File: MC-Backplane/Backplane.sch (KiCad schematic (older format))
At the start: 4 parts

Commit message: added reverse polarity protection circuit and fuse
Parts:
- removed R?: R_load, symbol Device:R_Small_US
- added F?: Fuse, symbol Device:Fuse
- D?: value BZX84C9V1-7-F -> Zener BZX84C9V1-7-F
- R?: value R1 -> 3k; footprint (none) -> Resistor_SMD:R_0201_0603Metric
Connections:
- net labels added: 24v
- net labels removed: +24V
- wire segments 14 -> 21
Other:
- note added: "Global reset to/from all cards and DSP\nFO enable b/w DSP and FO card only"
- note added: "If 0603 is used, minimum of 2.2k Ohm should be used.\n"
- note added: "Reverse Polarity Protection Circuit"
- moved on the sheet: D?, Q?, R?
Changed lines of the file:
@@
 F0 "GateDriveSlots" 50
 F1 "GateDriveSlots.sch" 50
+F2 "24vP" I L 2000 5350 50
 $EndSheet
 $Sheet
@@
 F0 "DeltaSigmaSlots" 50
 F1 "DeltaSigmasSlots.sch" 50
+F2 "24vP" I L 5000 5350 50
 $EndSheet
 $Sheet
-S 8750 5200 950  450
+S 8550 5250 950  450
 U 61E8CB26
 F0 "ADCSlots" 50
 F1 "ADCSlots.sch" 50
+F2 "24vP" I L 8550 5350 50
 $EndSheet
 $Sheet
-S 2200 2350 1000 450
+S 7900 2100 950  1900
 U 61E8CBE3
 F0 "DSPSlot" 50
 F1 "DSPSlot.sch" 50
+F2 "24vP" I L 7900 2200 50
 $EndSheet
-$Comp
-L power:+24V #PWR?
-U 1 1 61E8D5B6
-P 7350 1350
-F 0 "#PWR?" H 7350 1200 50  0001 C CNN
-F 1 "+24V" H 7365 1523 50  0000 C CNN
-F 2 "" H 7350 1350 50  0001 C CNN
-F 3 "" H 7350 1350 50  0001 C CNN
-	1    7350 1350
-	1    0    0    -1
-$EndComp
 $Comp
 L Device:Q_PMOS_DGS Q?
 U 1 1 61EB5F9E
-P 8500 1550
-F 0 "Q?" V 8842 1550 50  0000 C CNN
-F 1 "TSM3401CX RFG" V 8751 1550 50  0000 C CNN
-F 2 "" H 8700 1650 50  0001 C CNN
-F 3 "https://www.digikey.com/en/products/detail/taiwan-semiconductor-corporation/TSM3401CX-RFG/7360318" H 8500 1550 50  0001 C CNN
-	1    8500 1550
+P 2850 2300
+F 0 "Q?" V 3192 2300 50  0000 C CNN
+F 1 "TSM3401CX RFG" V 3101 2300 50  0000 C CNN
+F 2 "" H 3050 2400 50  0001 C CNN
+F 3 "https://www.digikey.com/en/products/detail/taiwan-semiconductor-corporation/TSM3401CX-RFG/7360318" H 2850 2300 50  0001 C CNN
+	1    2850 2300
 	0    -1   -1   0
 $EndComp
@@
 L Device:D_Zener D?
 U 1 1 61EB8C1B
-P 9350 1750
-F 0 "D?" V 9304 1830 50  0000 L CNN
-F 1 "BZX84C9V1-7-F" V 9395 1830 50  0000 L CNN
-F 2 "" H 9350 1750 50  0001 C CNN
-F 3 "https://www.digikey.com/en/products/detail/diodes-incorporated/BZX84C9V1-7-F/717755" H 9350 1750 50  0001 C CNN
-	1    9350 1750
+P 3700 2500
+F 0 "D?" V 3654 2580 50  0000 L CNN
+F 1 "Zener BZX84C9V1-7-F" V 3745 2580 50  0000 L CNN
+F 2 "" H 3700 2500 50  0001 C CNN
+F 3 "https://www.digikey.com/en/products/detail/diodes-incorporated/BZX84C9V1-7-F/717755" H 3700 2500 50  0001 C CNN
+	1    3700 2500
 	0    1    1    0
 $EndComp
 $Comp
 L Device:R_Small_US R?
-U 1 1 61EBA674
-P 10250 2100
-F 0 "R?" H 10318 2146 50  0000 L CNN
-F 1 "R_load" H 10318 2055 50  0000 L CNN
-F 2 "" H 10250 2100 50  0001 C CNN
-F 3 "~" H 10250 2100 50  0001 C CNN
-	1    10250 2100
-	1    0    0    -1
-$EndComp
-$Comp
-L Device:R_Small_US R?
 U 1 1 61EBB5D2
-P 8500 2400
-F 0 "R?" H 8568 2446 50  0000 L CNN
-F 1 "R1" H 8568 2355 50  0000 L CNN
-F 2 "" H 8500 2400 50  0001 C CNN
-F 3 "~" H 8500 2400 50  0001 C CNN
-	1    8500 2400
+P 2850 3150
+F 0 "R?" H 2918 3196 50  0000 L CNN
+F 1 "3k" H 2918 3105 50  0000 L CNN
+F 2 "Resistor_SMD:R_0201_0603Metric" H 2850 3150 50  0001 C CNN
+F 3 "~" H 2850 3150 50  0001 C CNN
+	1    2850 3150
 	1    0    0    -1
 $EndComp
 Wire Wire Line
-	8500 1750 8500 2000
+	2850 2500 2850 2750
 Wire Wire Line
-	9350 1900 9350 2000
+	3700 2650 3700 2750
 Wire Wire Line
-	9350 2000 8500 2000
-Connection ~ 8500 2000
+	3700 2750 2850 2750
+Connection ~ 2850 2750
 Wire Wire Line
-	8500 2000 8500 2300
+	2850 2750 2850 3050
 Wire Wire Line
-	9350 1600 9350 1450
+	3700 2350 3700 2200
 Wire Wire Line
-	9350 1450 8700 1450
+	3700 2200 3050 2200
+Connection ~ 3700 2200
 Wire Wire Line
-	9350 1450 10250 1450
-Wire Wire Line
-	10250 1450 10250 2000
-Connection ~ 9350 1450
-Wire Wire Line
-	8300 1450 7350 1450
-Wire Wire Line
-	7350 1450 7350 1350
-Wire Wire Line
-	10250 2750 8500 2750
-Wire Wire Line
-	8500 2750 8500 2500
-Wire Wire Line
-	10250 2200 10250 2750
-Wire Wire Line
-	8500 2750 8500 2850
-Connection ~ 8500 2750
+	2650 2200 2250 2200
 $Comp
-L power:GND #PWR?
+L power:GND #PWR0101
 U 1 1 61EBD36B
-P 8500 2850
-F 0 "#PWR?" H 8500 2600 50  0001 C CNN
-F 1 "GND" H 8505 2677 50  0000 C CNN
-F 2 "" H 8500 2850 50  0001 C CNN
-F 3 "" H 8500 2850 50  0001 C CNN
-	1    8500 2850
+P 2850 3600
+F 0 "#PWR0101" H 2850 3350 50  0001 C CNN
+F 1 "GND" H 2855 3427 50  0000 C CNN
+F 2 "" H 2850 3600 50  0001 C CNN
+F 3 "" H 2850 3600 50  0001 C CNN
+	1    2850 3600
 	1    0    0    -1
 $EndComp
-Text Notes 5800 3600 0    50   ~ 0
+Text Notes 800  1300 0    50   ~ 0
 RDS of PMOS needs to be really small like miliohms.\n\nDrain current needs to be larger than what the load requires.\nVDS needs to be larger than the source voltage by a significant amount. 24V so around  45V-60V.\n\nThe Zener diode needs a voltage rating of just under VDS of the mosfet. \n\nnot sure about the resistors.
+Wire Wire Line
+	2850 3250 2850 3600
+Text Notes 600  3000 0    50   ~ 0
+If 0603 is used, minimum of 2.2k Ohm should be used.\n
+Text GLabel 1700 2200 0    50   Input ~ 0
+24v
+$Comp
+L Device:Fuse F?
+U 1 1 61F00499
+P 2100 2200
+F 0 "F?" V 1903 2200 50  0000 C CNN
+F 1 "Fuse" V 1994 2200 50  0000 C CNN
+F 2 "" V 2030 2200 50  0001 C CNN
+F 3 "~" H 2100 2200 50  0001 C CNN
+	1    2100 2200
+	0    1    1    0
+$EndComp
+Wire Wire Line
+	1950 2200 1700 2200
+Text Notes 2250 1800 0    50   ~ 0
+Reverse Polarity Protection Circuit
+Text Notes 8500 900  0    50   ~ 0
+Global reset to/from all cards and DSP\nFO enable b/w DSP and FO card only
+Wire Wire Line
+	3700 2200 4750 2200
+Wire Wire Line
+	4750 2200 4750 4250
+Wire Wire Line
+	1200 4250 1200 5350
+Wire Wire Line
+	1200 5350 2000 5350
+Connection ~ 4750 4250
+Wire Wire Line
+	4750 4250 1200 4250
+Wire Wire Line
+	4750 5350 5000 5350
+Wire Wire Line
+	4750 4250 4750 4950
+Wire Wire Line
+	4750 4950 8150 4950
+Wire Wire Line
+	8150 4950 8150 5350
+Wire Wire Line
+	8150 5350 8550 5350
+Connection ~ 4750 4950
+Wire Wire Line
+	4750 4950 4750 5350
+Wire Wire Line
+	4750 2200 7900 2200
+Connection ~ 4750 2200
 $EndSCHEMATC

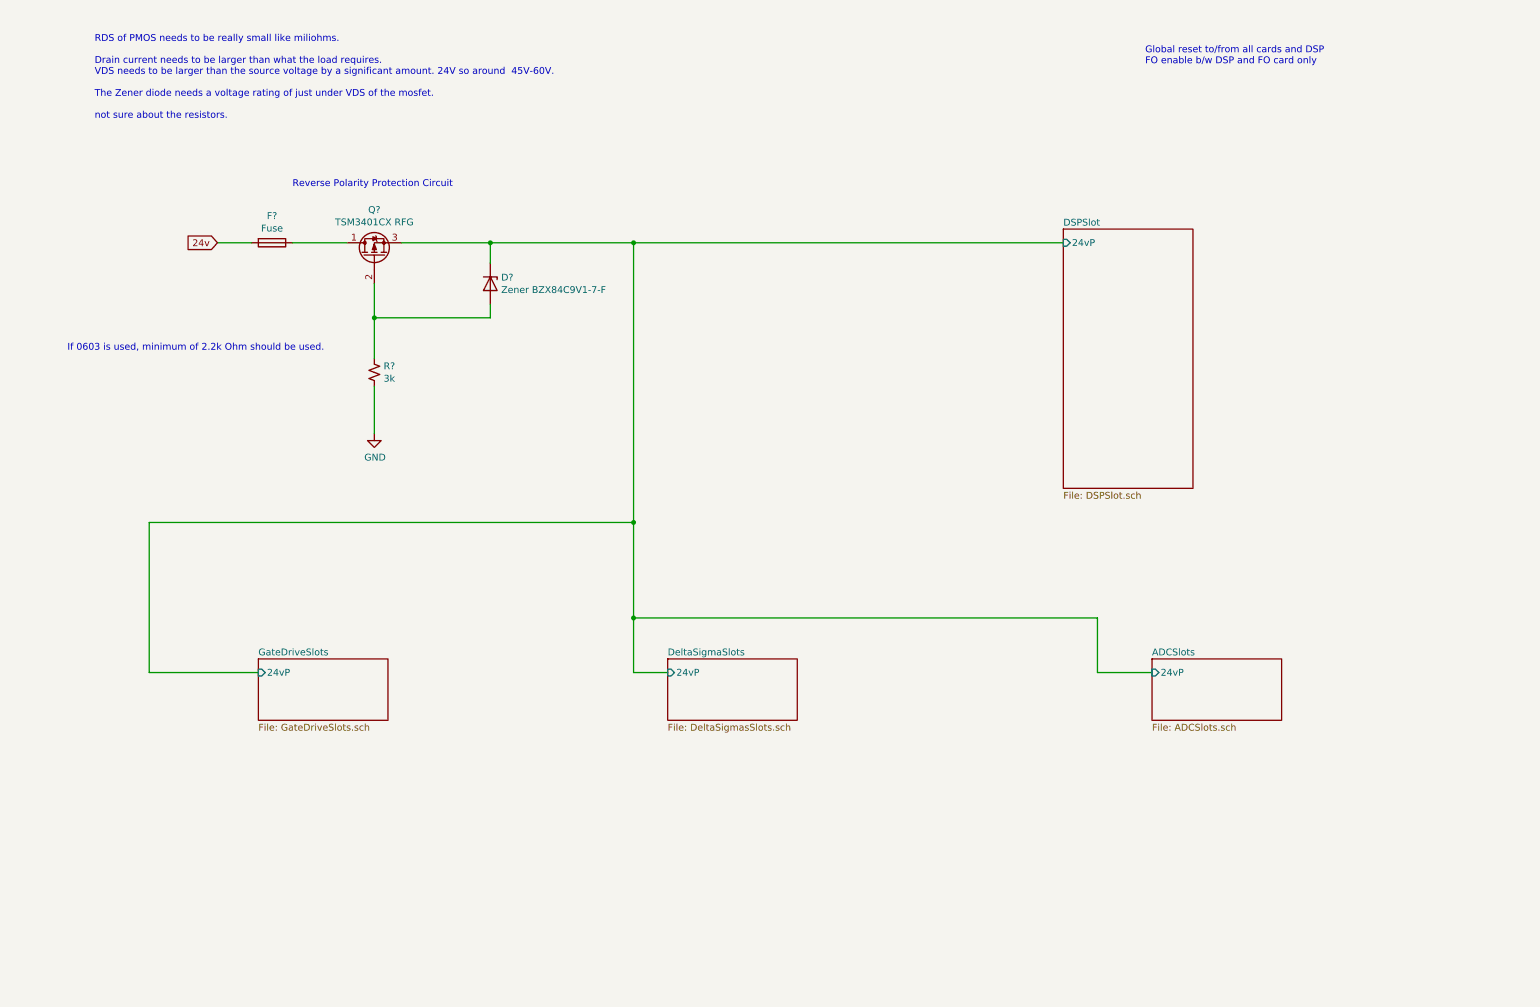
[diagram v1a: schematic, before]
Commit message: pmos swap, fuse cartridge, power conn
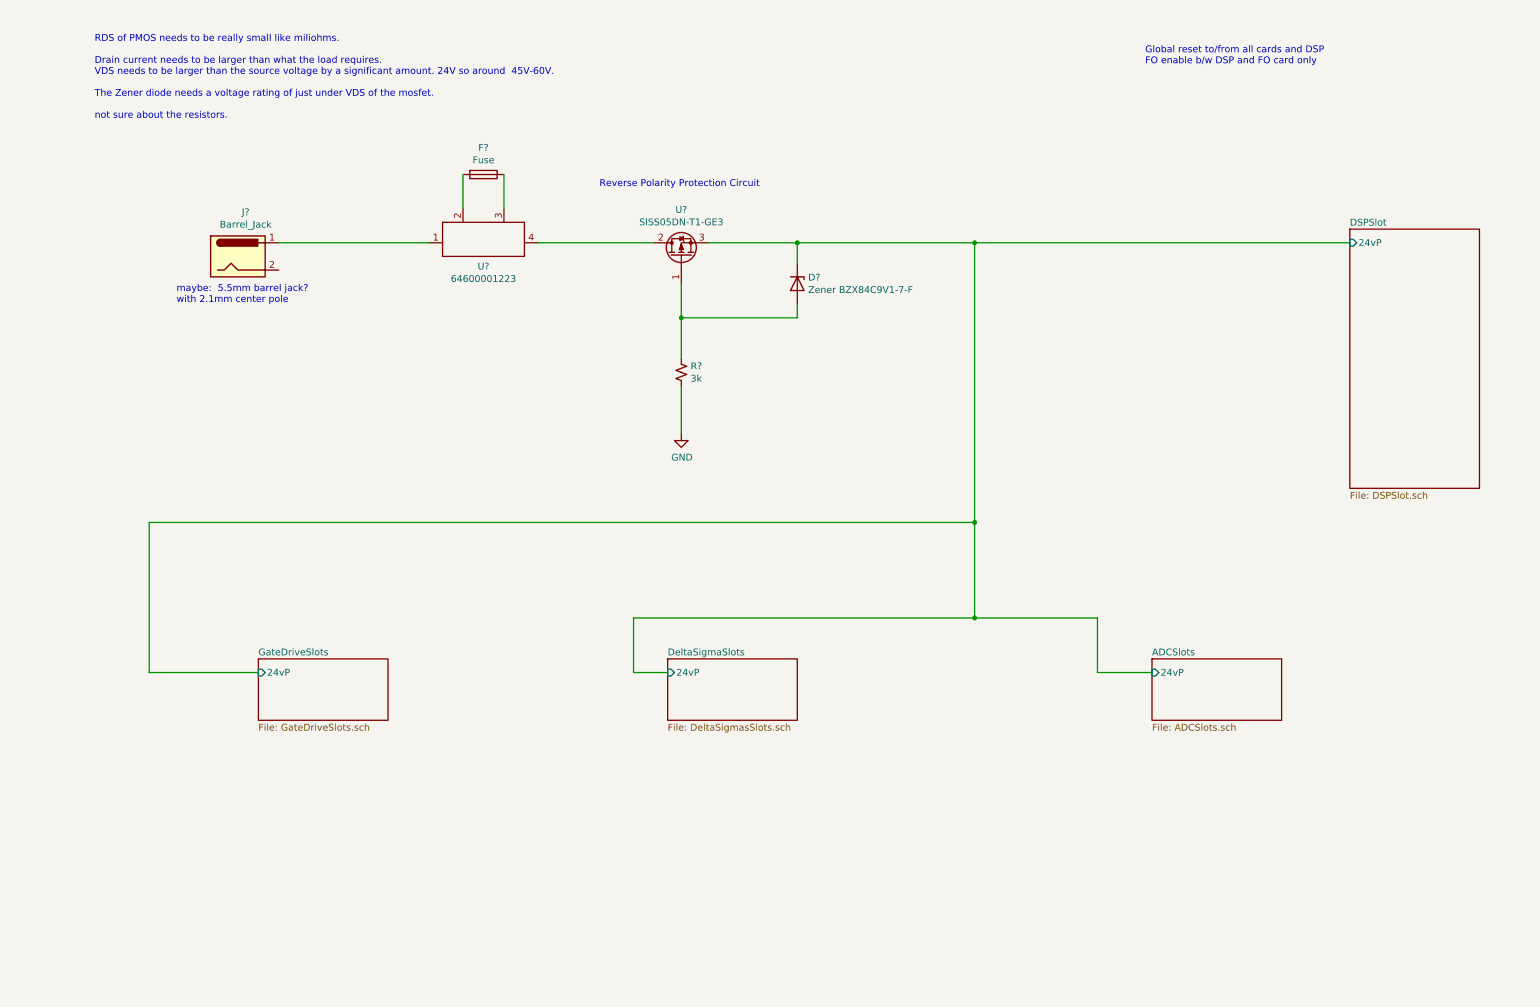
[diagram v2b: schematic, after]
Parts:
- removed F?: Fuse, symbol Device:Fuse
- removed Q?: TSM3401CX RFG, symbol Device:Q_PMOS_DGS
- added F?: Fuse, symbol Device:Fuse
- added J?: Barrel_Jack, symbol Connector:Barrel_Jack
- added U?: 64600001223, symbol MC-Backplane:64600001223
- added U?: SISS05DN-T1-GE3, symbol MC-Backplane:SISS05DN-T1-GE3
- R?: footprint Resistor_SMD:R_0201_0603Metric -> Resistor_SMD:R_1206_3216Metric
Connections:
- net ADCSlots/24vP: now also U?.3 (Source)
- net at D?.2 (A), R?.1: now also U?.1 (G)
- new net: J?.1, U?.1 (in)
- new net: F?.2, U?.2 (a)
- new net: F?.1, U?.3 (b)
- new net: U?.2 (Drain), U?.4 (out)
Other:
- note added: "maybe: 5.5mm barrel jack? \nwith 2.1mm center pole"
- note removed: "If 0603 is used, minimum of 2.2k Ohm should be used.\n"
- moved on the sheet: D?, R?
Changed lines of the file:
@@
 F2 "24vP" I L 8550 5350 50
 $EndSheet
-$Sheet
-S 7900 2100 950  1900
-U 61E8CBE3
-F0 "DSPSlot" 50
-F1 "DSPSlot.sch" 50
-F2 "24vP" I L 7900 2200 50
-$EndSheet
-$Comp
-L Device:Q_PMOS_DGS Q?
-U 1 1 61EB5F9E
-P 2850 2300
-F 0 "Q?" V 3192 2300 50  0000 C CNN
-F 1 "TSM3401CX RFG" V 3101 2300 50  0000 C CNN
-F 2 "" H 3050 2400 50  0001 C CNN
-F 3 "https://www.digikey.com/en/products/detail/taiwan-semiconductor-corporation/TSM3401CX-RFG/7360318" H 2850 2300 50  0001 C CNN
-	1    2850 2300
-	0    -1   -1   0
-$EndComp
 $Comp
 L Device:D_Zener D?
 U 1 1 61EB8C1B
-P 3700 2500
-F 0 "D?" V 3654 2580 50  0000 L CNN
-F 1 "Zener BZX84C9V1-7-F" V 3745 2580 50  0000 L CNN
-F 2 "" H 3700 2500 50  0001 C CNN
-F 3 "https://www.digikey.com/en/products/detail/diodes-incorporated/BZX84C9V1-7-F/717755" H 3700 2500 50  0001 C CNN
-	1    3700 2500
+P 5950 2500
+F 0 "D?" V 5904 2580 50  0000 L CNN
+F 1 "Zener BZX84C9V1-7-F" V 5995 2580 50  0000 L CNN
+F 2 "" H 5950 2500 50  0001 C CNN
+F 3 "https://www.digikey.com/en/products/detail/diodes-incorporated/BZX84C9V1-7-F/717755" H 5950 2500 50  0001 C CNN
+	1    5950 2500
 	0    1    1    0
 $EndComp
@@
 L Device:R_Small_US R?
 U 1 1 61EBB5D2
-P 2850 3150
-F 0 "R?" H 2918 3196 50  0000 L CNN
-F 1 "3k" H 2918 3105 50  0000 L CNN
-F 2 "Resistor_SMD:R_0201_0603Metric" H 2850 3150 50  0001 C CNN
-F 3 "~" H 2850 3150 50  0001 C CNN
-	1    2850 3150
+P 5100 3150
+F 0 "R?" H 5168 3196 50  0000 L CNN
+F 1 "3k" H 5168 3105 50  0000 L CNN
+F 2 "Resistor_SMD:R_1206_3216Metric" H 5100 3150 50  0001 C CNN
+F 3 "~" H 5100 3150 50  0001 C CNN
+	1    5100 3150
 	1    0    0    -1
 $EndComp
 Wire Wire Line
-	2850 2500 2850 2750
+	5100 2500 5100 2750
 Wire Wire Line
-	3700 2650 3700 2750
+	5950 2650 5950 2750
 Wire Wire Line
-	3700 2750 2850 2750
-Connection ~ 2850 2750
+	5950 2750 5100 2750
+Connection ~ 5100 2750
 Wire Wire Line
-	2850 2750 2850 3050
+	5100 2750 5100 3050
 Wire Wire Line
-	3700 2350 3700 2200
+	5950 2350 5950 2200
 Wire Wire Line
-	3700 2200 3050 2200
-Connection ~ 3700 2200
-Wire Wire Line
-	2650 2200 2250 2200
+	5950 2200 5300 2200
+Connection ~ 5950 2200
 $Comp
 L power:GND #PWR0101
 U 1 1 61EBD36B
-P 2850 3600
-F 0 "#PWR0101" H 2850 3350 50  0001 C CNN
-F 1 "GND" H 2855 3427 50  0000 C CNN
-F 2 "" H 2850 3600 50  0001 C CNN
-F 3 "" H 2850 3600 50  0001 C CNN
-	1    2850 3600
+P 5100 3600
+F 0 "#PWR0101" H 5100 3350 50  0001 C CNN
+F 1 "GND" H 5105 3427 50  0000 C CNN
+F 2 "" H 5100 3600 50  0001 C CNN
+F 3 "" H 5100 3600 50  0001 C CNN
+	1    5100 3600
 	1    0    0    -1
 $EndComp
@@
 RDS of PMOS needs to be really small like miliohms.\n\nDrain current needs to be larger than what the load requires.\nVDS needs to be larger than the source voltage by a significant amount. 24V so around  45V-60V.\n\nThe Zener diode needs a voltage rating of just under VDS of the mosfet. \n\nnot sure about the resistors.
 Wire Wire Line
-	2850 3250 2850 3600
-Text Notes 600  3000 0    50   ~ 0
-If 0603 is used, minimum of 2.2k Ohm should be used.\n
-Text GLabel 1700 2200 0    50   Input ~ 0
-24v
-$Comp
-L Device:Fuse F?
-U 1 1 61F00499
-P 2100 2200
-F 0 "F?" V 1903 2200 50  0000 C CNN
-F 1 "Fuse" V 1994 2200 50  0000 C CNN
-F 2 "" V 2030 2200 50  0001 C CNN
-F 3 "~" H 2100 2200 50  0001 C CNN
-	1    2100 2200
-	0    1    1    0
-$EndComp
-Wire Wire Line
-	1950 2200 1700 2200
-Text Notes 2250 1800 0    50   ~ 0
+	5100 3250 5100 3600
+Text Notes 4500 1800 0    50   ~ 0
 Reverse Polarity Protection Circuit
 Text Notes 8500 900  0    50   ~ 0
 Global reset to/from all cards and DSP\nFO enable b/w DSP and FO card only
 Wire Wire Line
-	3700 2200 4750 2200
-Wire Wire Line
-	4750 2200 4750 4250
-Wire Wire Line
 	1200 4250 1200 5350
 Wire Wire Line
 	1200 5350 2000 5350
-Connection ~ 4750 4250
-Wire Wire Line
-	4750 4250 1200 4250
 Wire Wire Line
 	4750 5350 5000 5350
 Wire Wire Line
-	4750 4250 4750 4950
-Wire Wire Line
-	4750 4950 8150 4950
+	4750 4950 7250 4950
 Wire Wire Line
 	8150 4950 8150 5350
 Wire Wire Line
 	8150 5350 8550 5350
-Connection ~ 4750 4950
 Wire Wire Line
 	4750 4950 4750 5350
+$Comp
+L MC-Backplane:64600001223 U?
+U 1 1 61F13696
+P 3650 2400
+F 0 "U?" H 3650 2427 50  0000 C CNN
+F 1 "64600001223" H 3650 2336 50  0000 C CNN
+F 2 "" H 3650 2400 50  0001 C CNN
+F 3 "https://www.littelfuse.com/~/media/electronics/datasheets/fuse_blocks/littelfuse_fuse_block_646_datasheet.pdf.pdf" H 3650 2400 50  0001 C CNN
+	1    3650 2400
+	1    0    0    -1
+$EndComp
 Wire Wire Line
-	4750 2200 7900 2200
-Connection ~ 4750 2200
+	4050 2200 4900 2200
+Wire Wire Line
+	5950 2200 7250 2200
+Wire Wire Line
+	1200 4250 7250 4250
+Wire Wire Line
+	7250 4250 7250 2200
+Connection ~ 7250 2200
+Wire Wire Line
+	7250 2200 10000 2200
+Wire Wire Line
+	7250 4250 7250 4950
+Connection ~ 7250 4250
+Connection ~ 7250 4950
+Wire Wire Line
+	7250 4950 8150 4950
+$Comp
+L Connector:Barrel_Jack J?
+U 1 1 61F21CB0
+P 1850 2300
+F 0 "J?" H 1907 2625 50  0000 C CNN
+F 1 "Barrel_Jack" H 1907 2534 50  0000 C CNN
+F 2 "" H 1900 2260 50  0001 C CNN
+F 3 "~" H 1900 2260 50  0001 C CNN
+	1    1850 2300
+	1    0    0    -1
+$EndComp
+Wire Wire Line
+	2150 2200 3250 2200
+$Comp
+L Device:Fuse F?
+U 1 1 61F2B17A
+P 3650 1700
+F 0 "F?" V 3453 1700 50  0000 C CNN
+F 1 "Fuse" V 3544 1700 50  0000 C CNN
+F 2 "" V 3580 1700 50  0001 C CNN
+F 3 "~" H 3650 1700 50  0001 C CNN
+	1    3650 1700
+	0    1    1    0
+$EndComp
+Wire Wire Line
+	3500 1700 3500 1950
+Wire Wire Line
+	3800 1950 3800 1700
+Text Notes 1400 2650 0    50   ~ 0
+maybe:  5.5mm barrel jack? \nwith 2.1mm center pole
+$Comp
+L MC-Backplane:SISS05DN-T1-GE3 U?
+U 1 1 61F2E911
+P 5600 2200
+F 0 "U?" V 5842 2700 50  0000 C CNN
+F 1 "SISS05DN-T1-GE3" V 5751 2700 50  0000 C CNN
+F 2 "" H 5600 2200 50  0001 C CNN
+F 3 "" H 5600 2200 50  0001 C CNN
+	1    5600 2200
+	0    -1   -1   0
+$EndComp
+$Sheet
+S 10000 2100 950  1900
+U 61E8CBE3
+F0 "DSPSlot" 50
+F1 "DSPSlot.sch" 50
+F2 "24vP" I L 10000 2200 50
+$EndSheet
 $EndSCHEMATC
